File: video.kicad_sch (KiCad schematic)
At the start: 55 parts, among them IC10 2318, IC11 MC14053, IC14 74LS86, IC21 74LS123, IC22 74LS00, IC23 74LS74, IC27 74LS20, IC28 74LS393, IC29 74LS393, IC30 74LS32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

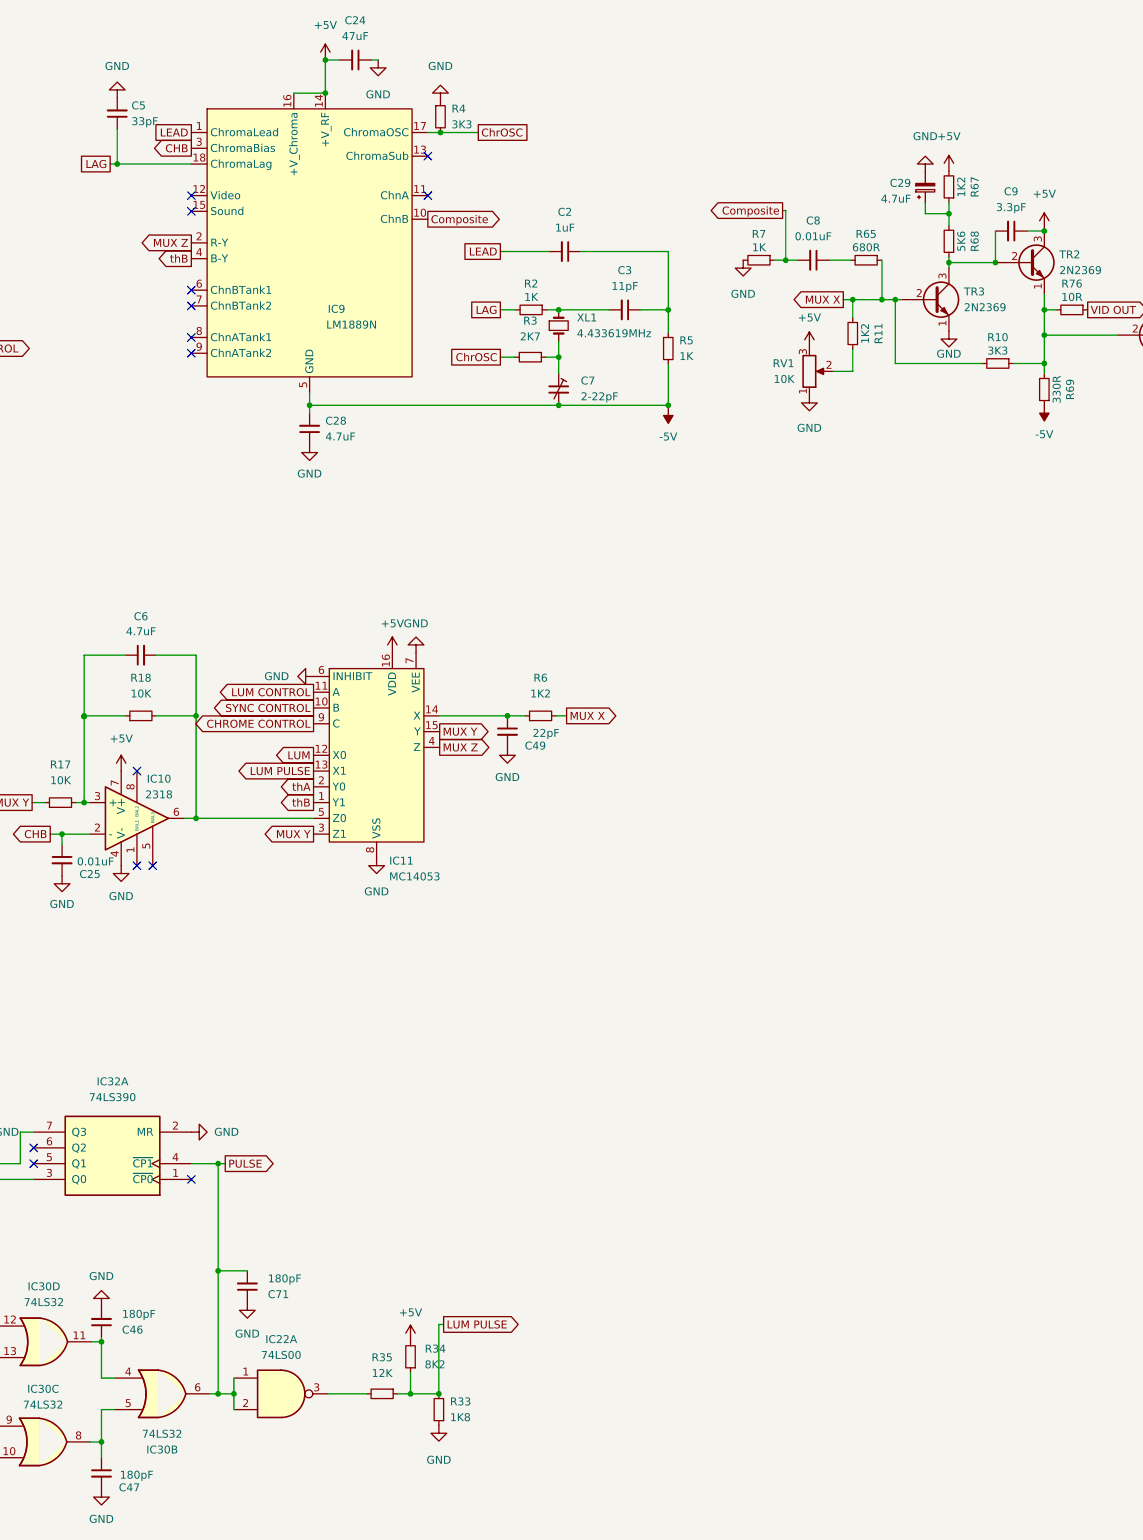
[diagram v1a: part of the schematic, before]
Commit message: validate component values
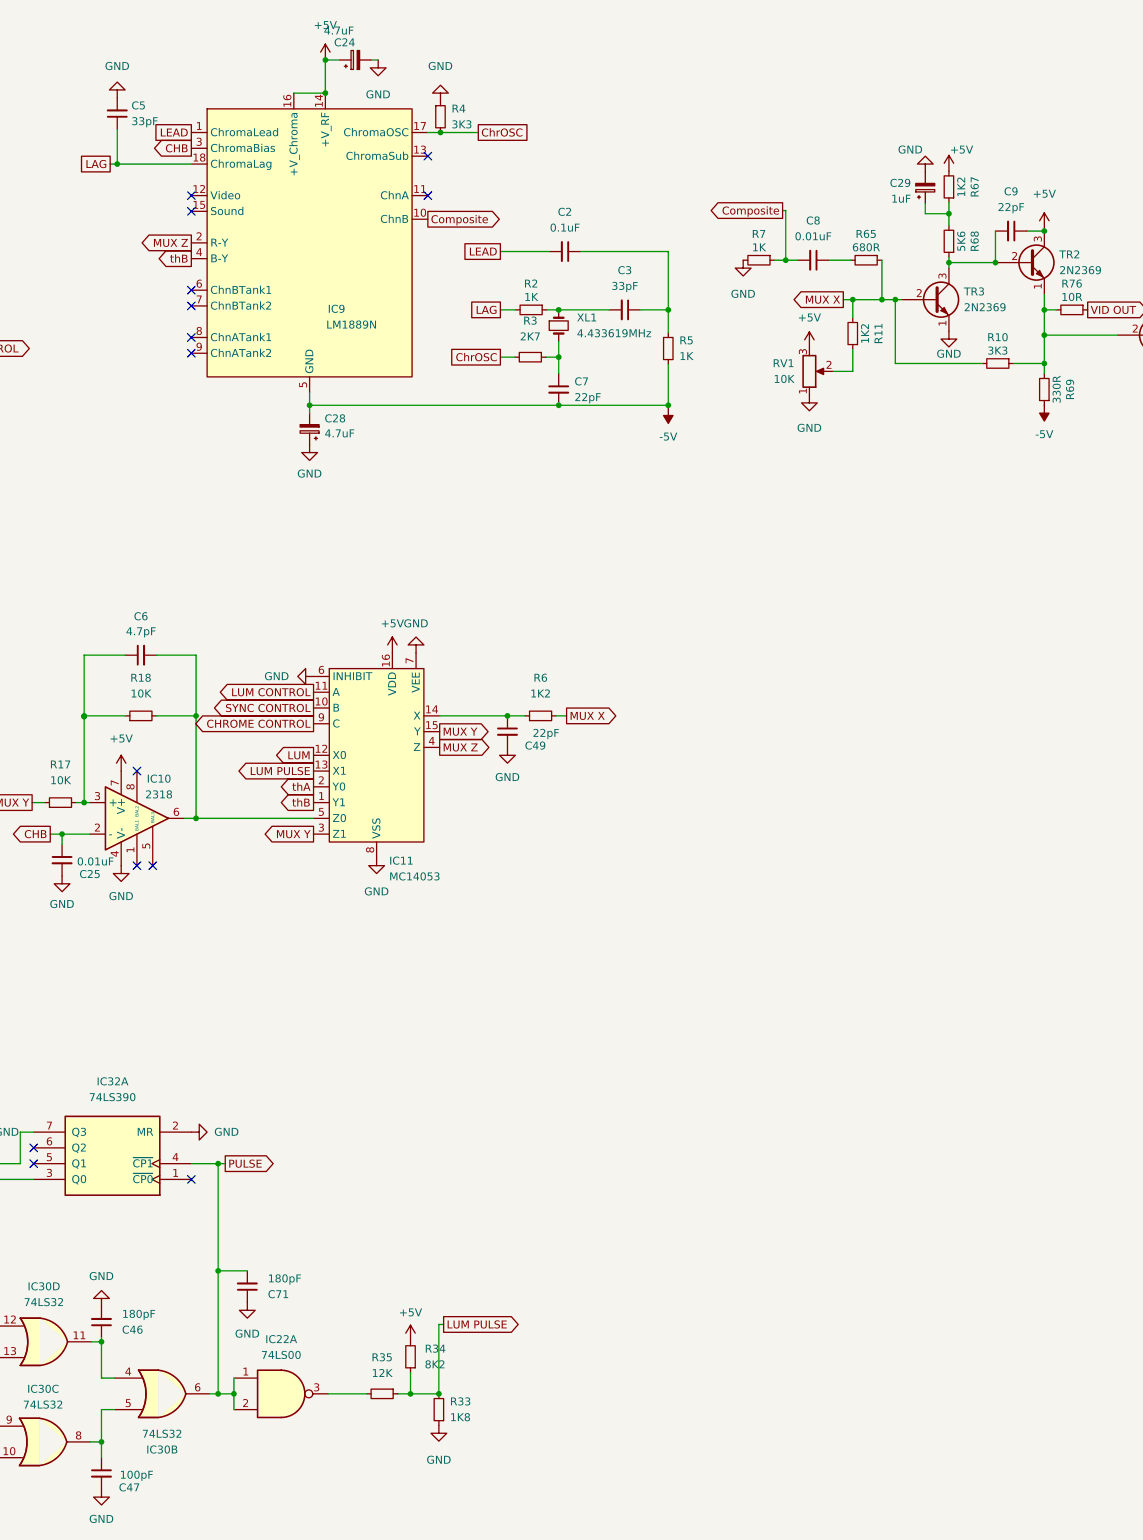
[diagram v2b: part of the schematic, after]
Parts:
- removed C24: 47uF, Capacitor_THT:C_Disc_D3.0mm_W2.0mm_P2.50mm, symbol Device:C_Small
- removed C28: 4.7uF, Capacitor_THT:C_Disc_D3.0mm_W2.0mm_P2.50mm, symbol Device:C_Small
- removed C7: 2-22pF, Potentiometer_THT:Potentiometer_ACP_CA6-H2,5_Horizontal, symbol Device:C_Trim_Small
- added C24, C28: 4.7uF, Capacitor_THT:CP_Radial_D5.0mm_P2.50mm, symbol Device:C_Polarized_Small
- added C7: 22pF, Capacitor_THT:C_Disc_D3.0mm_W2.0mm_P2.50mm, symbol Device:C_Small
- C2: value 1uF -> 0.1uF; footprint Capacitor_THT:C_Disc_D3.0mm_W2.0mm_P2.50mm -> Capacitor_THT:C_Disc_D4.3mm_W1.9mm_P5.00mm
- C25: footprint Capacitor_THT:C_Disc_D3.0mm_W2.0mm_P2.50mm -> Capacitor_THT:C_Disc_D4.3mm_W1.9mm_P5.00mm
- C29: value 4.7uF -> 1uF; DigiKey (none) -> 732-8966-1-ND
- C3: value 11pF -> 33pF
- C47: value 180pF -> 100pF
- C6: value 4.7uF -> 4.7pF
- C8: footprint Capacitor_THT:C_Disc_D3.0mm_W2.0mm_P2.50mm -> Capacitor_THT:C_Disc_D4.7mm_W2.5mm_P5.00mm
- C9: value 3.3pF -> 22pF
- PL6: DigiKey (none) -> 2057-LHD-09-TS-ND; Toby (none) -> WH396-09S-010
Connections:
- net +5V: now also C24.1
- net -5V: now also C28.2, C7.2
- net GND: now also C24.2, C28.1
- net at R3.1, XL1.2: now also C7.1

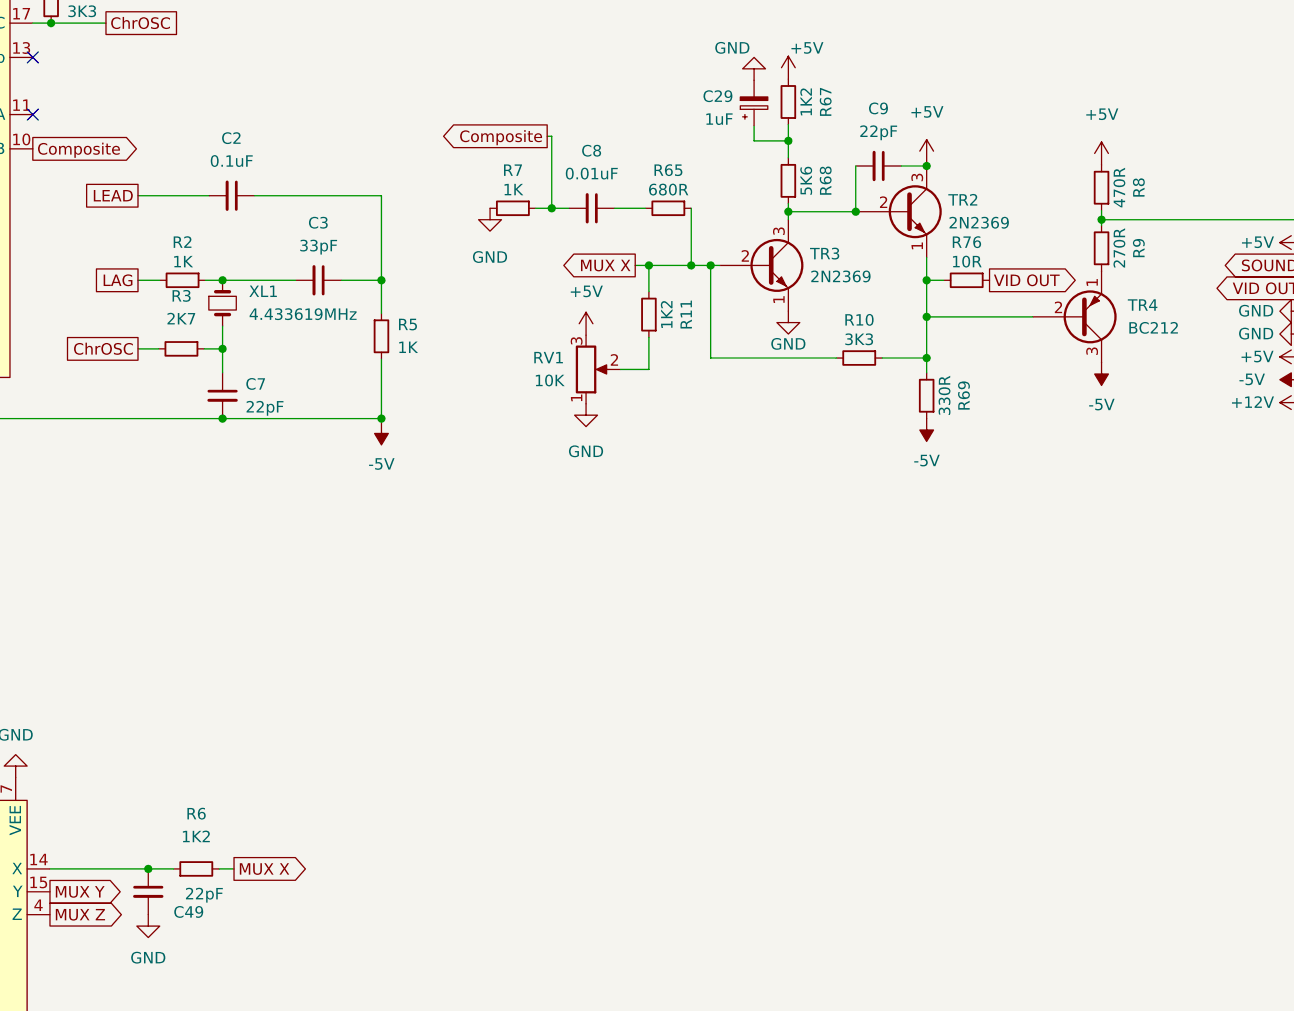
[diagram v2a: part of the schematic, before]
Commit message: resitor values pt1
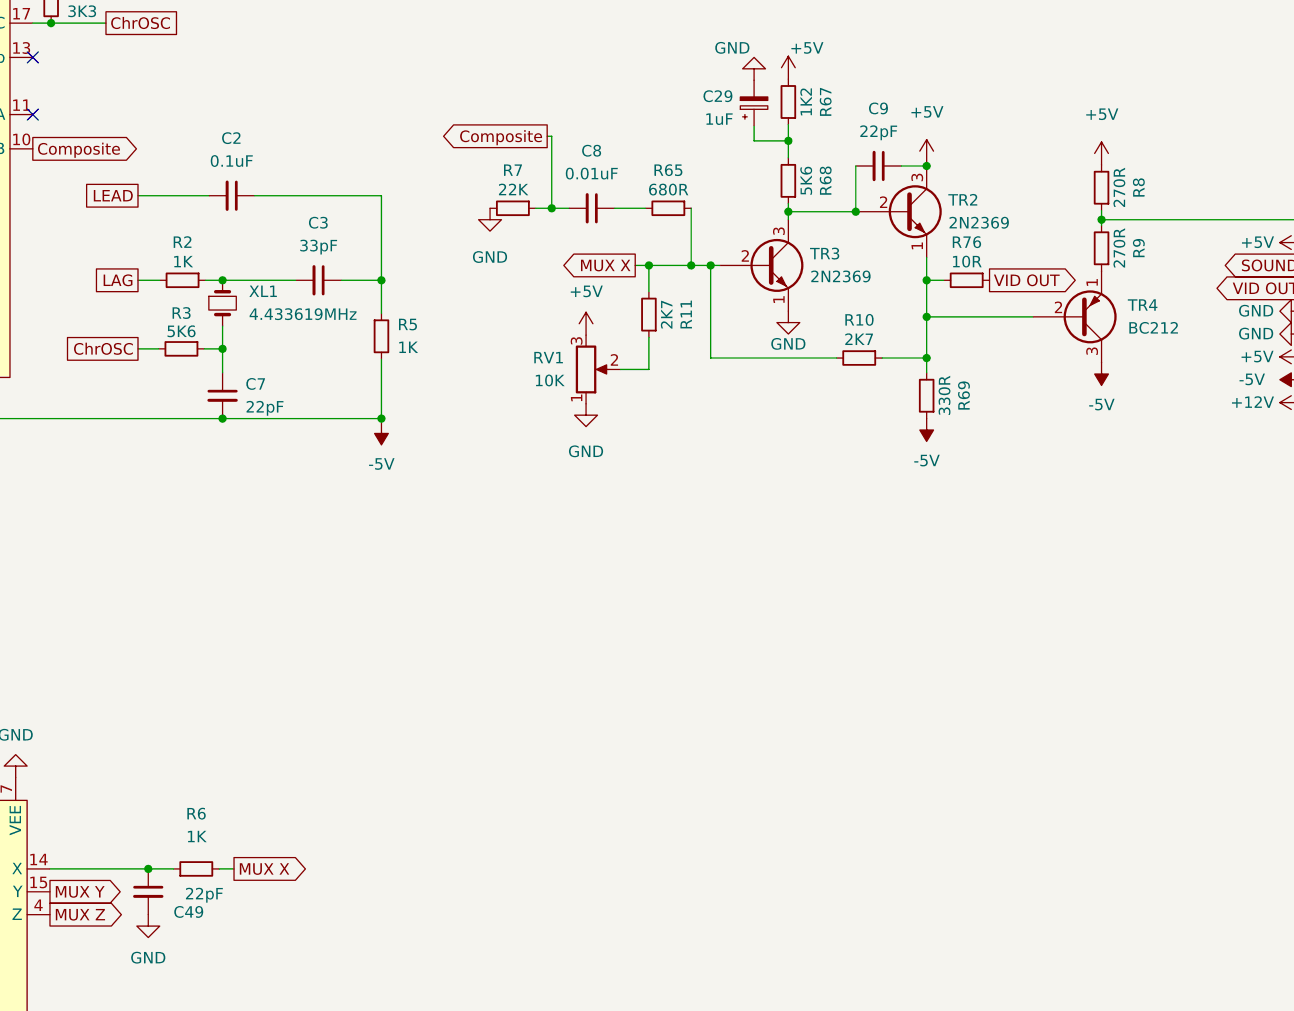
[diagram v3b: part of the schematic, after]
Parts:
- R10: value 3K3 -> 2K7
- R11: value 1K2 -> 2K7
- R3: value 2K7 -> 5K6
- R6: value 1K2 -> 1K
- R7: value 1K -> 22K
- R8: value 470R -> 270R
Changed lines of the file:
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@@
     (in_bom yes) (on_board yes)
     (property "Reference" "R8" (id 0) (at 325.501 73.533 90))
-    (property "Value" "470R" (id 1) (at 323.342 73.533 90))
+    (property "Value" "270R" (id 1) (at 323.342 73.533 90))
     (property "Footprint" "Resistor_THT:R_Axial_DIN0207_L6.3mm_D2.5mm_P10.16mm_Horizontal" (id 2) (at 321.31 73.533 0)
       (effects (font (size 1.27 1.27)) hide)
@@
     (in_bom yes) (on_board yes)
     (property "Reference" "R7" (id 0) (at 255.905 71.628 90))
-    (property "Value" "1K" (id 1) (at 255.905 73.787 90))
+    (property "Value" "22K" (id 1) (at 255.905 73.787 90))
     (property "Footprint" "Resistor_THT:R_Axial_DIN0207_L6.3mm_D2.5mm_P10.16mm_Horizontal" (id 2) (at 255.905 75.819 0)
       (effects (font (size 1.27 1.27)) hide)
@@
     (in_bom yes) (on_board yes) (fields_autoplaced)
     (property "Reference" "R6" (id 0) (at 220.726 143.129 90))
-    (property "Value" "1K2" (id 1) (at 220.726 145.669 90))
+    (property "Value" "1K" (id 1) (at 220.726 145.669 90))
     (property "Footprint" "Resistor_THT:R_Axial_DIN0207_L6.3mm_D2.5mm_P10.16mm_Horizontal" (id 2) (at 220.726 149.225 0)
       (effects (font (size 1.27 1.27)) hide)
@@
     (in_bom yes) (on_board yes)
     (property "Reference" "R10" (id 0) (at 294.386 88.265 90))
-    (property "Value" "3K3" (id 1) (at 294.386 90.424 90))
+    (property "Value" "2K7" (id 1) (at 294.386 90.424 90))
     (property "Footprint" "Resistor_THT:R_Axial_DIN0207_L6.3mm_D2.5mm_P10.16mm_Horizontal" (id 2) (at 294.386 92.456 0)
       (effects (font (size 1.27 1.27)) hide)
@@
     (in_bom yes) (on_board yes)
     (property "Reference" "R11" (id 0) (at 275.209 87.63 90))
-    (property "Value" "1K2" (id 1) (at 273.05 87.63 90))
+    (property "Value" "2K7" (id 1) (at 273.05 87.63 90))
     (property "Footprint" "Resistor_THT:R_Axial_DIN0207_L6.3mm_D2.5mm_P10.16mm_Horizontal" (id 2) (at 271.018 87.63 0)
       (effects (font (size 1.27 1.27)) hide)
@@
   )
   (symbol (lib_id "Device:R_Small") (at 219.075 91.44 270) (unit 1)
-    (in_bom yes) (on_board yes) (fields_autoplaced)
-    (property "Reference" "R3" (id 0) (at 219.075 85.598 90))
-    (property "Value" "2K7" (id 1) (at 219.075 88.138 90))
+    (in_bom yes) (on_board yes)
+    (property "Reference" "R3" (id 0) (at 219.075 87.503 90))
+    (property "Value" "5K6" (id 1) (at 219.075 89.535 90))
     (property "Footprint" "Resistor_THT:R_Axial_DIN0207_L6.3mm_D2.5mm_P10.16mm_Horizontal" (id 2) (at 219.075 91.44 0)
       (effects (font (size 1.27 1.27)) hide)

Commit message: complete component revision
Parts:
- R33: value 1K8 -> 3K3
- R34: value 8K2 -> 6K8
- R35: value 12K -> 15K
- R65: value 680R -> 2K7
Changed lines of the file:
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@@
       (effects (font (size 1.27 1.27)) (justify right))
     )
-    (property "Value" "8K2" (id 1) (at 202.057 253.7459 0)
+    (property "Value" "6K8" (id 1) (at 202.057 253.7459 0)
       (effects (font (size 1.27 1.27)) (justify right))
     )
@@
     (in_bom yes) (on_board yes) (fields_autoplaced)
     (property "Reference" "R35" (id 0) (at 195.199 252.603 90))
-    (property "Value" "12K" (id 1) (at 195.199 255.143 90))
+    (property "Value" "15K" (id 1) (at 195.199 255.143 90))
     (property "Footprint" "Resistor_THT:R_Axial_DIN0207_L6.3mm_D2.5mm_P10.16mm_Horizontal" (id 2) (at 195.199 258.445 0)
       (effects (font (size 1.27 1.27)) hide)
@@
       (effects (font (size 1.27 1.27)) (justify right))
     )
-    (property "Value" "1K8" (id 1) (at 206.121 262.2549 0)
+    (property "Value" "3K3" (id 1) (at 206.121 262.2549 0)
       (effects (font (size 1.27 1.27)) (justify right))
     )
@@
     (in_bom yes) (on_board yes)
     (property "Reference" "R65" (id 0) (at 273.177 71.628 90))
-    (property "Value" "680R" (id 1) (at 273.177 73.787 90))
+    (property "Value" "2K7" (id 1) (at 273.177 73.787 90))
     (property "Footprint" "Resistor_THT:R_Axial_DIN0207_L6.3mm_D2.5mm_P10.16mm_Horizontal" (id 2) (at 273.177 75.819 0)
       (effects (font (size 1.27 1.27)) hide)

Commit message: cross-reference items to suppliers
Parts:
- IC14: value 74LS86 -> 74LS86N
- IC21: value 74LS123 -> 74LS123N
- IC21: value 74LS123 -> 74LS123N; DigiKey (none) -> 296-1636-5-ND
- IC22: value 74LS00 -> 74LS00N; DigiKey (none) -> 296-1626-ND
- IC22: value 74LS00 -> 74LS00N
- IC23: value 74LS74 -> 74ALS74N
- IC23: value 74LS74 -> 74ALS74N; DigiKey (none) -> 296-1504-5-ND
- IC27: value 74LS20 -> 74LS20N; DigiKey (none) -> 296-3670-5-ND
- IC27: value 74LS20 -> 74LS20N
- IC28, IC29: value 74LS393 -> 74LS393N; DigiKey (none) -> 296-1665-5-ND
- IC28, IC29: value 74LS393 -> 74LS393N
- IC30: value 74LS32 -> 74LS32N
- IC30: value 74LS32 -> 74LS32N; DigiKey (none) -> 296-1658-5-ND
- IC32: DigiKey (none) -> 296-26516-5-ND
